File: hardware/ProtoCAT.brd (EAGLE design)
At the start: 59.7 x 53.3 mm, 54 parts, among them U1 ARDUINO, U3 TB6612FNG

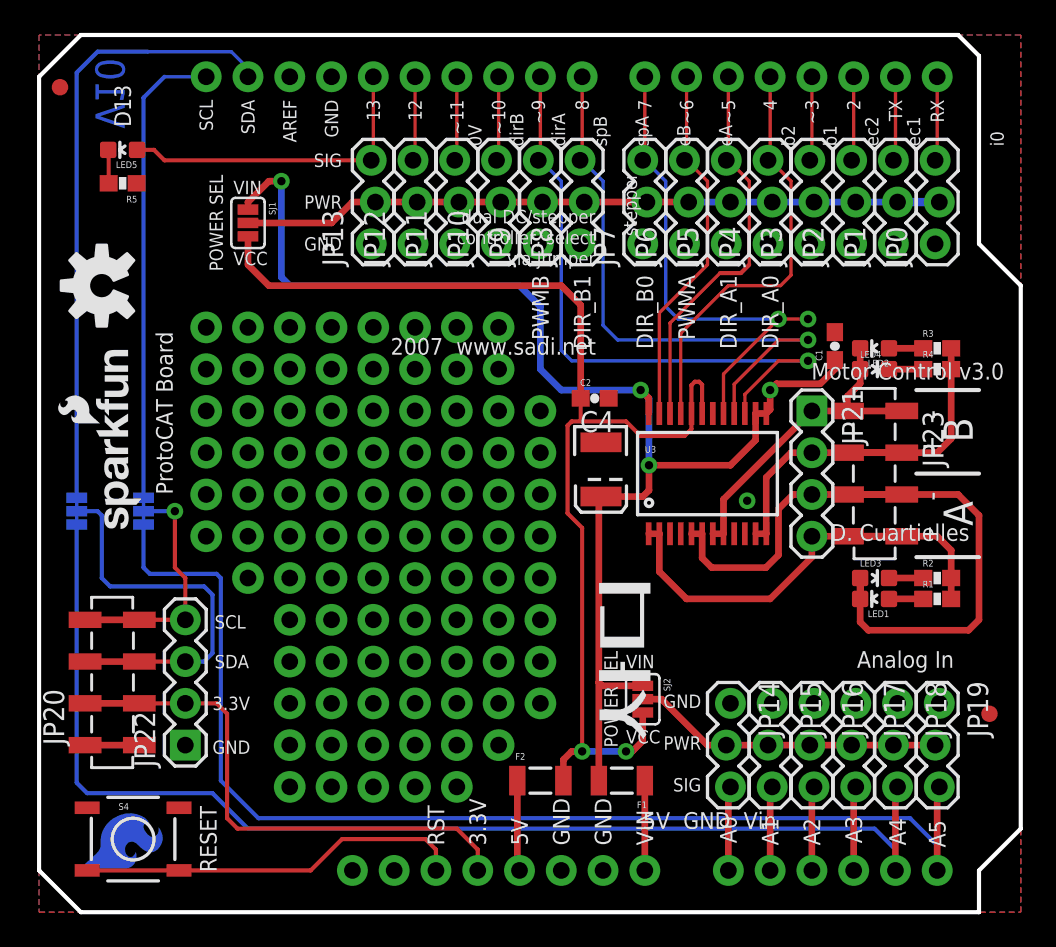
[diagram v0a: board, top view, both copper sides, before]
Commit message: Initial Commit
Updated / Changed ProtoCAT to include an XBee header
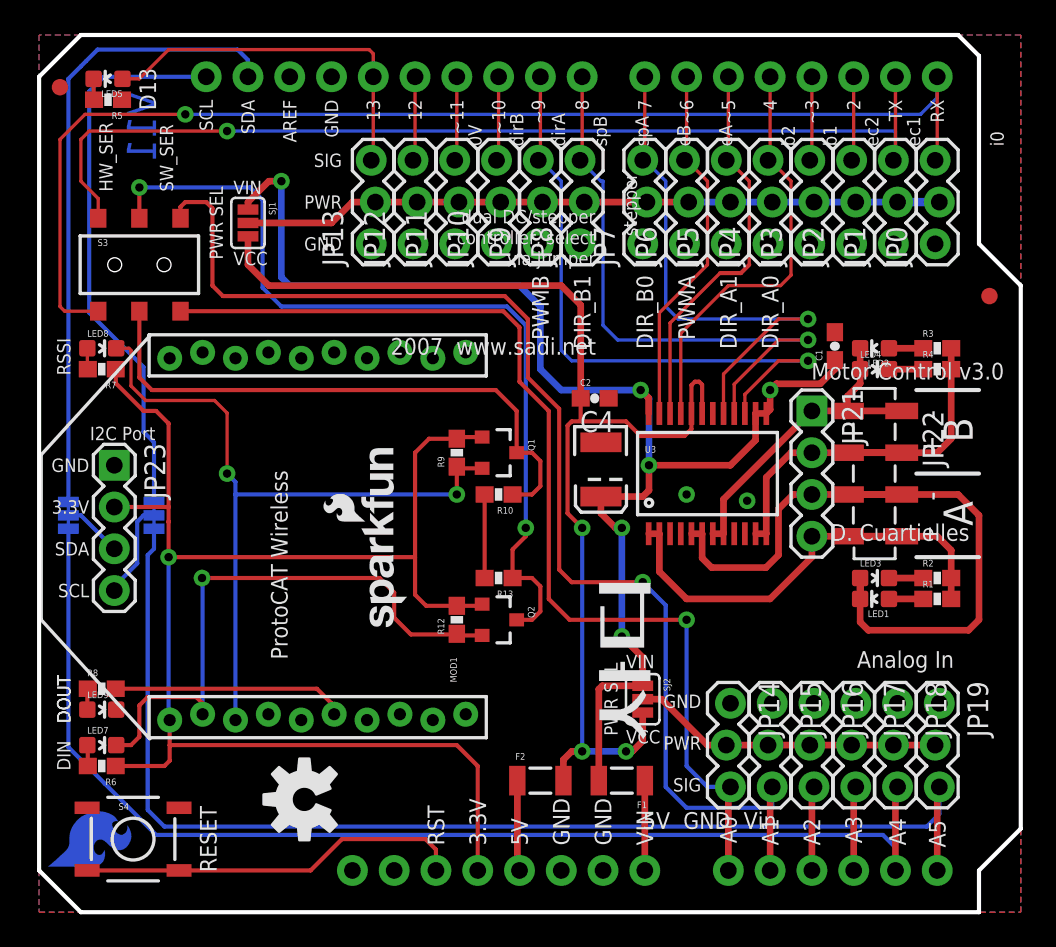
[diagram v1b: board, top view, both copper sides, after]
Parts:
- removed JP20: (no value), SparkFun-Connectors:1X04_SMD_STRAIGHT_COMBO
- added LED7: Red, SparkFun-LED:LED-0603
- added LED8, LED9: Green, SparkFun-LED:LED-0603
- added MOD1: XBEE-1XBEE-1_LOCK, SparkFun-RF:XBEE-1_LOCK
- added Q1, Q2: MOSFET-NCHANNELSMD, SparkFun-DiscreteSemi:SOT23-3
- added R10, R12, R13, R6, R7, R8, R9: 1k, SparkFun-Resistors:0603-RES
- added S3: DPDT, SparkFun-Electromechanical:AYZ0202
- FRAME1: value FRAME-LETTER -> FRAME-LEDGER
- JP22: device SparkFun-Connectors:1X04 -> SparkFun-Connectors:1X04_SMD_STRAIGHT_COMBO
- JP23: device SparkFun-Connectors:1X04_SMD_STRAIGHT_COMBO -> SparkFun-Connectors:1X04
- moved JP22 46.6 mm to (50.8, 30.5), turned to 270 degrees
- moved JP23 46.3 mm to (4.57, 27.2)
- moved LOGO1 33.6 mm to (16.1, 6.86)
- moved FID2 25.4 mm to (57.8, 37.5)
- moved FRAME1 17.6 mm to (6.35, -21.6)
- moved LOGO2 17.2 mm to (22.5, 16.9)
- moved LOGO4 8.98 mm to (52.1, 27.9), turned to 270 degrees
- moved R5 5.16 mm to (4.19, 49.4)
- moved LED5 4.41 mm to (4.19, 50.7)
- moved LOGO3 1.91 mm to (0.25, 2.41)
- moved SJ4 0.68 mm to (6.99, 24.1)
- moved SJ3 0.57 mm to (1.78, 24.1)
- turned U$1 to 90 degrees
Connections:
- net N$20 renamed BIN2
- removed net A0: JP14.3, U1.A0
- removed net A1: JP15.3, U1.A1
- removed net D0: JP0.3, U1.RX
- removed net D1: JP1.3, U1.TX
- new net 5V: R10.2, R13.2
- new net A0/SW_RXI: JP14.3, S3.6, U1.A0
- new net A1/SW_TXO: JP15.3, S3.3, U1.A1
- new net D0_RXI: JP0.3, S3.4, U1.RX
- new net D1_TXO: JP1.3, S3.1, U1.TX
- new net DIN: LED8.C, MOD1.3, Q1.2, R9.1
- new net DOUT: LED7.C, MOD1.2, Q2.2, R12.1
- new net N$22: LED7.A, R6.2
- new net N$43: LED8.A, R7.2
- new net N$44: LED9.A, R8.1
- new net RSSI: MOD1.6, R8.2
- new net XBEE_RESET: MOD1.5
- new net XBEE_RXI: Q2.3, R13.1, S3.2
- new net XBEE_TXO: Q1.3, R10.1, S3.5
- net 3.3V: now also JP23.2, MOD1.1, Q1.1, Q2.1, R12.2, R6.1, R7.1, R9.2; no longer JP20.2, JP22.2
- net AOUT1: now also JP22.4; no longer JP23.4
- net AOUT2: now also JP22.3; no longer JP23.3
- net BOUT1: now also JP22.2; no longer JP23.2
- net BOUT2: now also JP22.1; no longer JP23.1
- net GND: now also JP23.1, LED9.C, MOD1.10; no longer JP20.1, JP22.1
- net SCL_I2C_PORT: now also JP23.4; no longer JP20.4, JP22.4
- net SDA_I2C_PORT: now also JP23.3; no longer JP20.3, JP22.3
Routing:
- net A1/SW_TXO: track 0.00 -> 75.4 mm, vias 0 -> 1
- net D0_RXI: track 0.00 -> 73.4 mm, vias 0 -> 1
- net A0/SW_RXI: track 0.00 -> 64.4 mm, vias 0 -> 1
- net D1_TXO: track 0.00 -> 61.9 mm, vias 0 -> 1
- net 3.3V: track 32.5 -> 90.5 mm, vias 0 -> 1
- net XBEE_RXI: track 0.00 -> 52.7 mm, vias 0 -> 2
- net DIN: track 0.00 -> 45.3 mm, vias 0 -> 2
- net DOUT: track 0.00 -> 36.1 mm, vias 0 -> 1
- net XBEE_TXO: track 0.00 -> 35.4 mm
- net SDA_I2C_PORT: track 20.8 -> 3.64 mm
- net RSSI: track 0.00 -> 14.2 mm
- net SCL_I2C_PORT: track 14.9 -> 5.94 mm, vias 1 -> 0
- net SCL: track 28.7 -> 34.1 mm
- net A0: track 5.13 -> 0.00 mm
- net D1: track 5.13 -> 0.00 mm
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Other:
- board text added: "DIN"
- board text added: "DOUT"
- board text added: "HW_SER"
- board text added: "I2C Port"
- board text added: "PWR SEL"
- board text added: "ProtoCAT Wireless"
- board text added: "RSSI"
- board text added: "SW_SER"
- board text added: "V11"
- board text removed: "POWER SEL"
- board text removed: "ProtoCAT Board"
- board text removed: "V10"
